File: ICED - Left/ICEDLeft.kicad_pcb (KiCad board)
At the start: 2 copper layers, 175.4 x 145 mm, 162 parts, among them P1 Conn_ARM_JTAG_SWD_10, P2 DX07S024XJ1R1100, P3 CONN_17, P4 692121130100, P5 RGB Out, Q1 TC1264, U1 MK20DX256VLH7, U2 IS31FL3737-QFLS4-TR, X1 CRYSTAL

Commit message: More routing
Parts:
- C18, C19, C20, C21, C6, C8, C9, R12, R3, R4, R5, R8: moved to B.Cu
- moved R5 37.0 mm to (101.6, 130.7), turned to 180 degrees
- moved R3 37.0 mm to (100.2, 130.7), turned to 180 degrees
- moved R4 30.5 mm to (97.8, 122.3)
- moved R8 17.1 mm to (97.1, 78.0), turned to 90 degrees
- moved C18 9.52 mm to (100.2, 69.3), turned to 90 degrees
- moved C20 9.22 mm to (101.9, 78.0)
- moved C21 9.08 mm to (99.6, 78.0)
- moved C9 8.99 mm to (100.7, 78.0)
- moved C6 8.69 mm to (100.2, 70.2), turned to 90 degrees
- moved C19 4.53 mm to (108.2, 75.3), turned to 0 degrees
- moved C8 4.09 mm to (106.4, 75.3), turned to 0 degrees
- moved R12 3.58 mm to (102.7, 75.8), turned to 270 degrees
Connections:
- U2 pad 21: /mcu/ledmatrix_2/Row4A -> /mcu/ledmatrix_2/Row3B
- U2 pad 22: /mcu/ledmatrix_2/Row4B -> /mcu/ledmatrix_2/Row4A
- U2 pad 23: /mcu/ledmatrix_2/Row4C -> /mcu/ledmatrix_2/Row4B
- U2 pad 24: /mcu/ledmatrix_2/Row5A -> /mcu/ledmatrix_2/Row4C
- U2 pad 25: /mcu/ledmatrix_2/Row5B -> /mcu/ledmatrix_2/Row5A
- U2 pad 27: (no net) -> /mcu/ledmatrix_2/Row5B
- U2 pad 29: /mcu/ledmatrix_2/GND -> VSS
- U2 pad 36: /mcu/ledmatrix_2/GND -> VSS
- U2 pad 4: /mcu/ledmatrix_2/GND -> VSS
- U2 pad 40: /mcu/ledmatrix_2/GND -> VSS
- U2 pad 41: /mcu/ledmatrix_2/GND -> VSS
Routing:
- net VSS: track 422.6 -> 612.9 mm, vias 9 -> 17
- net /mcu/ledmatrix_2/Blue3: track 139.7 -> 286.5 mm, vias 6 -> 10
- net /mcu/ledmatrix_2/Green3: track 136.3 -> 281.1 mm, vias 6 -> 10
- net /mcu/ledmatrix_2/Red3: track 124.8 -> 257.8 mm, vias 6 -> 10
- net /mcu/SDB: track 0.00 -> 106.0 mm, vias 0 -> 4
- net /mcu/ledmatrix_2/Blue2: track 248.1 -> 343.8 mm, vias 10 -> 11
- net /mcu/SDA0: track 52.4 -> 135.9 mm, vias 3 -> 6
- net /mcu/SCL0: track 53.5 -> 135.7 mm, vias 3 -> 6
- net /mcu/ledmatrix_2/Green2: track 237.0 -> 316.3 mm, vias 10 -> 11
- net /mcu/RGBIN: track 76.1 -> 0.46 mm, vias 2 -> 0
- net /mcu/ledmatrix_2/Row2B: track 1.27 -> 65.7 mm, vias 1 -> 2
- net /mcu/ledmatrix_2/Row4B: track 0.00 -> 44.9 mm
- net VDD: track 265.9 -> 301.7 mm, vias 7 -> 12
- net /mcu/ledmatrix_2/GND: track 21.9 -> 0.00 mm
- net /mcu/ledmatrix_2/Green4: track 139.8 -> 118.8 mm, vias 9 -> 7
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
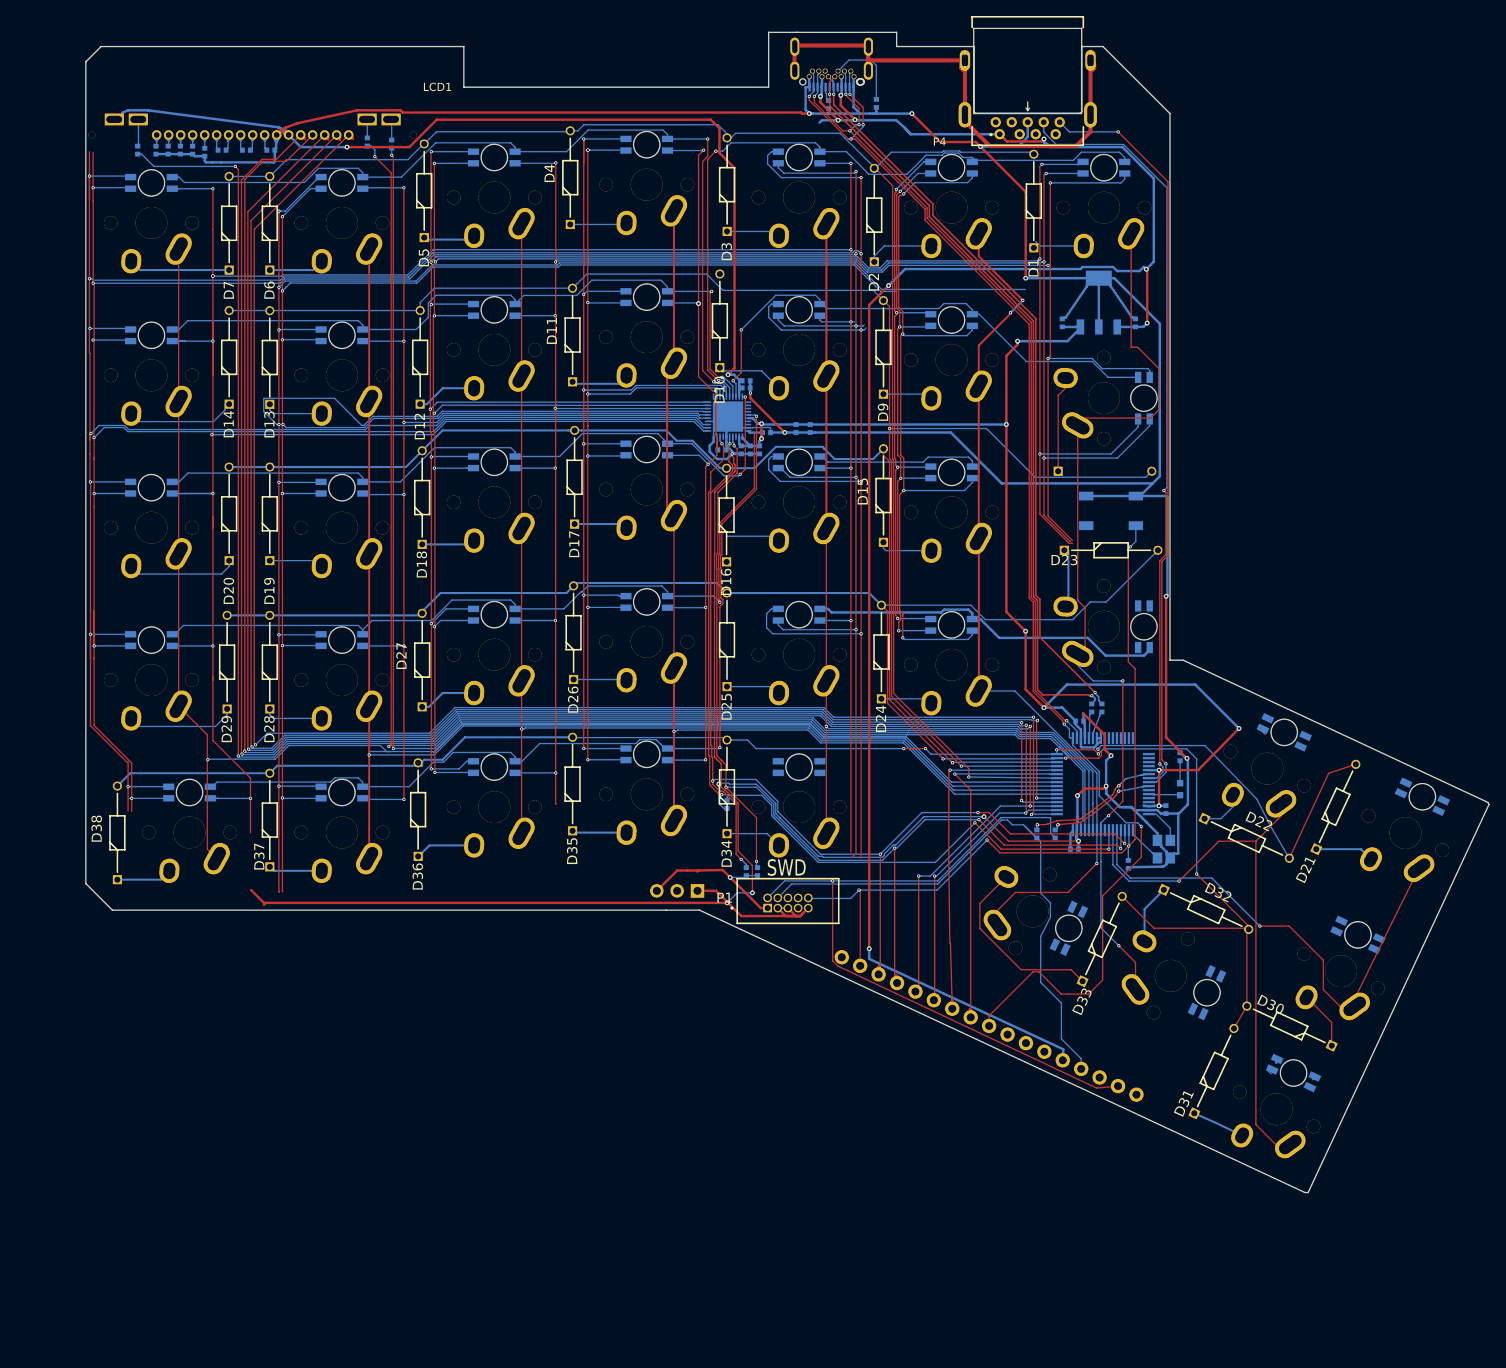
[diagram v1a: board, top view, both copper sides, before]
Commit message: Most non-thumb routing finished
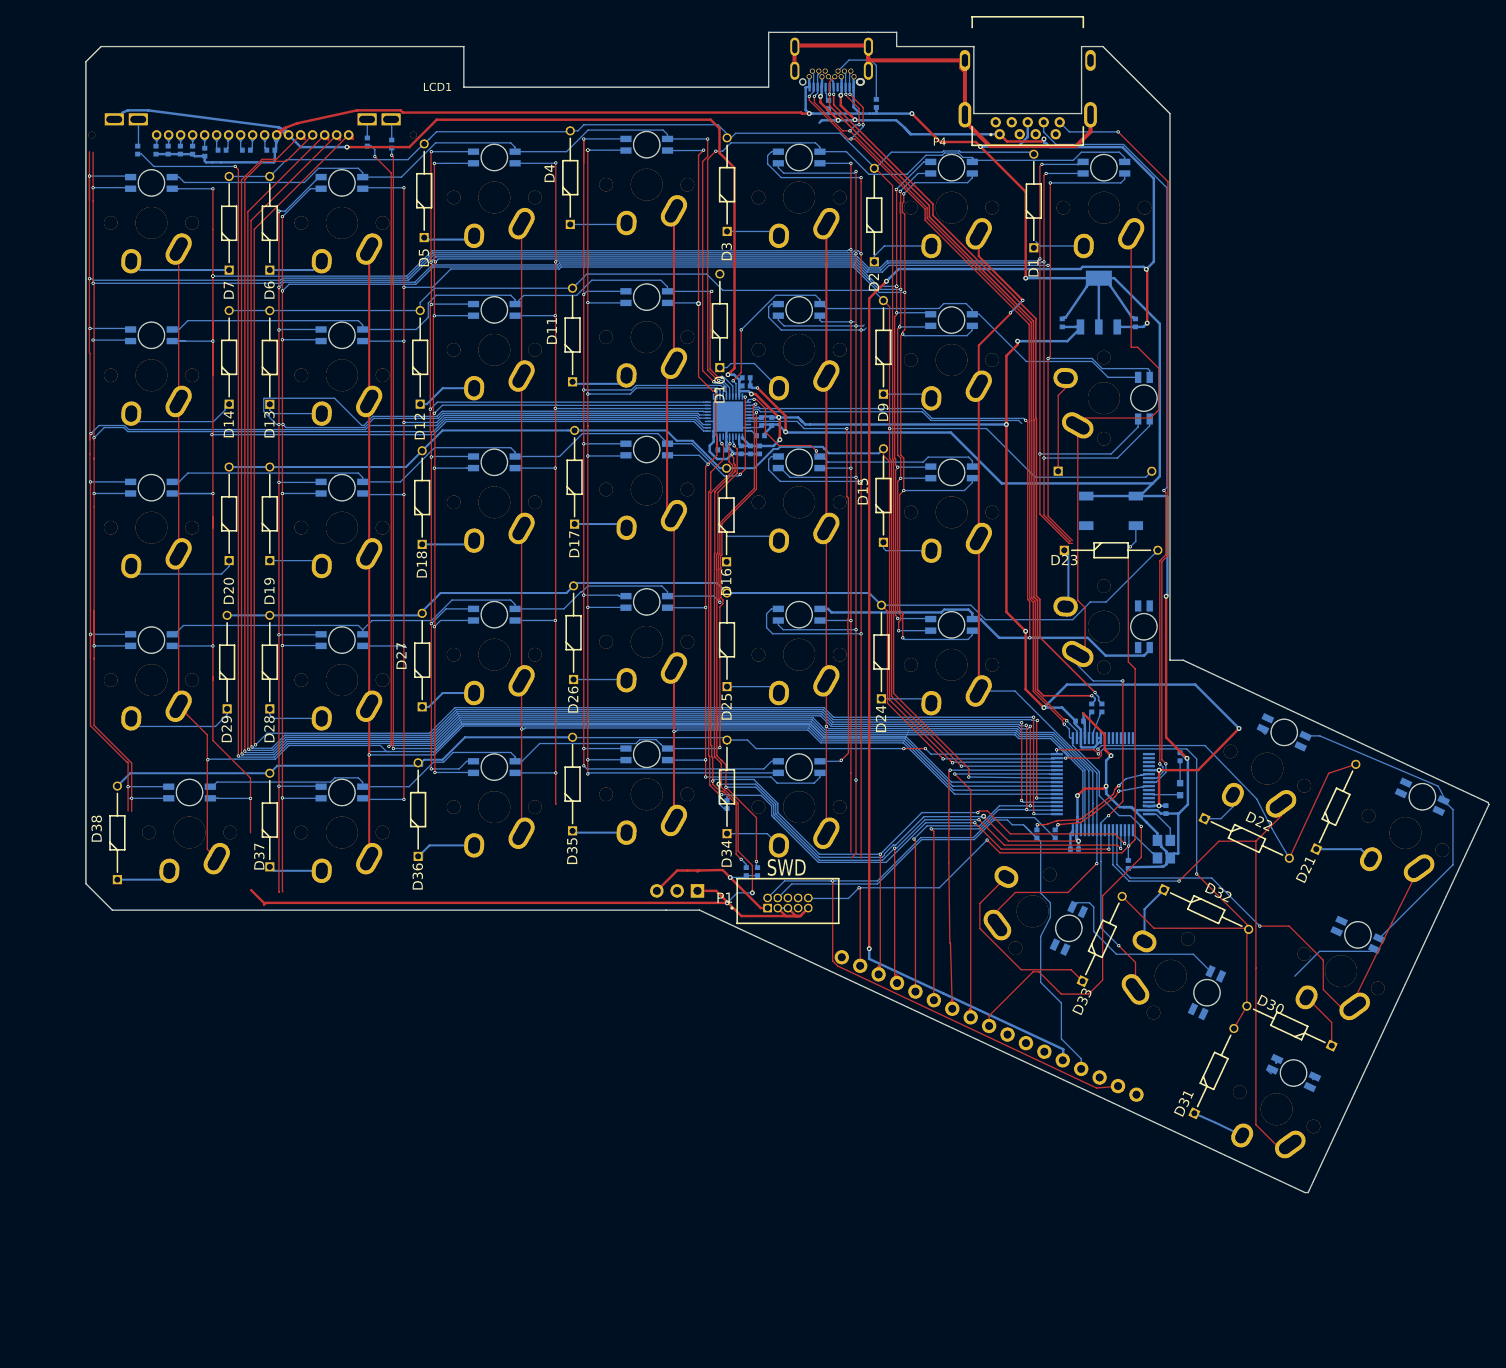
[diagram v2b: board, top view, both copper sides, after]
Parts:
- LCD1: value NHD-C12832A1Z -> VAL**
- moved C19 4.90 mm to (103.4, 74.4)
- moved C8 4.41 mm to (102.1, 74.4)
- moved R12 0.84 mm to (102.0, 76.2)
- moved C18 0.38 mm to (100.2, 69.0)
- moved C6 0.25 mm to (100.2, 70.0)
- turned LED30 to 335 degrees
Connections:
- LED31 pad 1: /mcu/ledmatrix_2/Red4 -> /mcu/ledmatrix_2/Red1
- LED31 pad 2: /mcu/ledmatrix_2/Green4 -> /mcu/ledmatrix_2/Green1
- LED31 pad 3: /mcu/ledmatrix_2/Blue4 -> /mcu/ledmatrix_2/Blue1
- LED32 pad 1: /mcu/ledmatrix_2/Red3 -> /mcu/ledmatrix_2/Red2
- LED32 pad 2: /mcu/ledmatrix_2/Green3 -> /mcu/ledmatrix_2/Green2
- LED32 pad 3: /mcu/ledmatrix_2/Blue3 -> /mcu/ledmatrix_2/Blue2
- LED33 pad 1: /mcu/ledmatrix_2/Red2 -> /mcu/ledmatrix_2/Red3
- LED33 pad 2: /mcu/ledmatrix_2/Green2 -> /mcu/ledmatrix_2/Green3
- LED33 pad 3: /mcu/ledmatrix_2/Blue2 -> /mcu/ledmatrix_2/Blue3
- LED34 pad 1: /mcu/ledmatrix_2/Red1 -> /mcu/ledmatrix_2/Red4
- LED34 pad 2: /mcu/ledmatrix_2/Green1 -> /mcu/ledmatrix_2/Green4
- LED34 pad 3: /mcu/ledmatrix_2/Blue1 -> /mcu/ledmatrix_2/Blue4
- P4 pad S4: /GND -> (no net)
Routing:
- net /mcu/ledmatrix_2/Row5B: track 0.69 -> 81.2 mm, vias 0 -> 2
- net /mcu/ledmatrix_2/Row4C: track 0.00 -> 76.4 mm
- net /mcu/ledmatrix_2/Red2: track 236.3 -> 301.0 mm, vias 10 -> 12
- net /mcu/ledmatrix_2/Row4B: track 44.9 -> 107.8 mm, vias 0 -> 2
- net /mcu/ledmatrix_2/Blue4: track 125.0 -> 152.0 mm, vias 6 -> 7
- net /mcu/ledmatrix_2/Green4: track 118.8 -> 144.0 mm, vias 7 -> 8
- net /mcu/ledmatrix_2/Red4: track 103.8 -> 121.0 mm, vias 6 -> 7
- net /mcu/ledmatrix_2/Blue2: track 343.8 -> 327.4 mm, vias 11 -> 13
- net /mcu/ledmatrix_2/Row3B: track 20.5 -> 35.0 mm, vias 0 -> 2
- net /mcu/ledmatrix_2/Red3: track 257.8 -> 269.2 mm
- net VDD: track 301.7 -> 311.3 mm, vias 12 -> 13
- net /GND: track 64.3 -> 57.0 mm
- net /mcu/ledmatrix_2/Row4A: track 97.6 -> 102.4 mm, vias 1 -> 2
- net VSS: track 612.9 -> 616.9 mm
- net /mcu/SCLK: track 227.8 -> 231.4 mm
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
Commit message: Routed and DRC passes
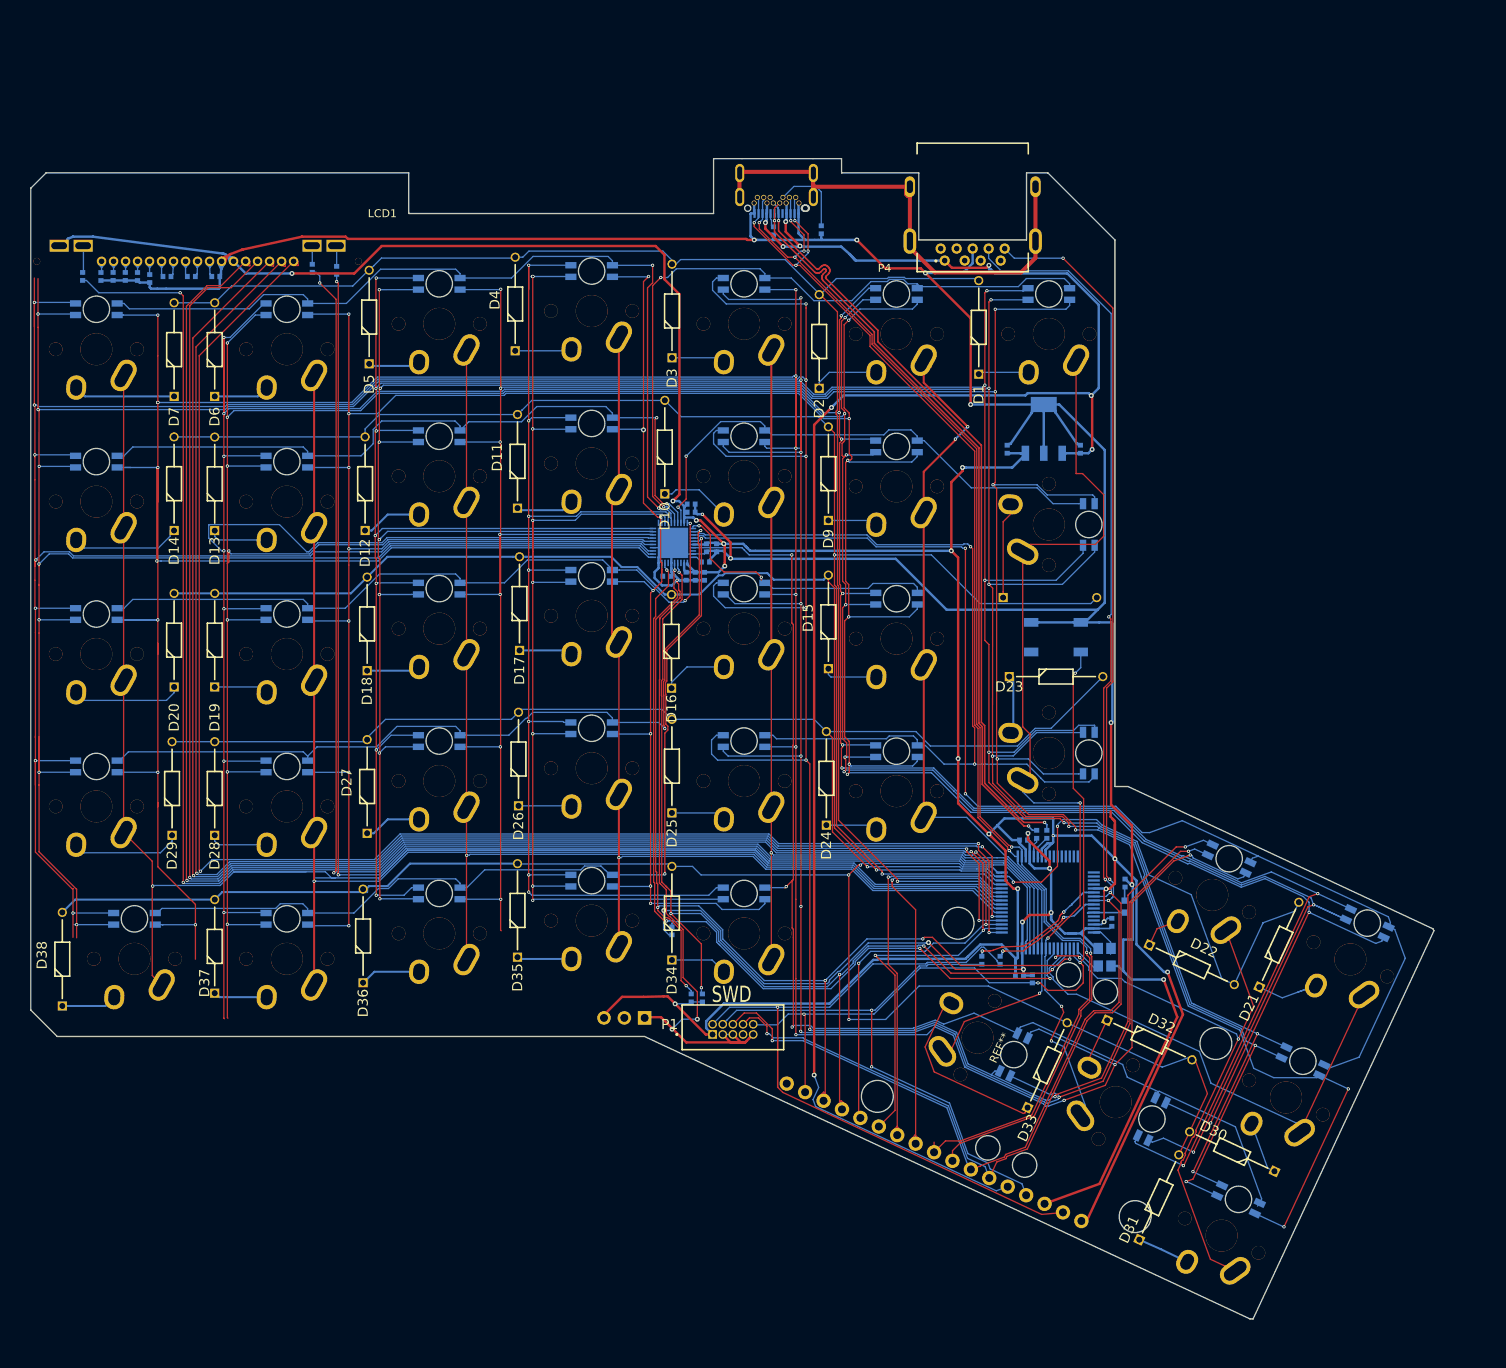
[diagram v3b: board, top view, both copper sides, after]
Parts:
- added REF**: Stabilizer_Cherry_MX_2u, prettylib:Stabilizer_Cherry_MX_2u, F.Cu at (129.1, 151.5)
- added STAB1: Stabilizer_Cherry_MX_2u, prettylib:Stabilizer_Cherry_MX_2u, F.Cu at (146.4, 159.5)
- LCD1: value VAL** -> NHD-C12832A1Z
- moved C5 18.7 mm to (136.0, 144.1), turned to 0 degrees
- moved D21 18.7 mm to (164.3, 145.1)
- moved D32 17.8 mm to (145.3, 149.3)
- moved D30 17.3 mm to (166.2, 168.2)
- moved S26 17.2 mm to (80.9, 117.8)
- moved R5 17.2 mm to (94.7, 146.5)
- moved LED1 17.2 mm to (138.0, 58.5)
- moved C13 17.2 mm to (25.6, 56.6)
- moved D12 17.2 mm to (52.6, 88.1)
- moved S31 17.2 mm to (159.6, 176.2)
- moved D33 17.2 mm to (135.4, 160.2)
- moved S25 17.2 mm to (99.9, 119.4)
- moved P2 17.2 mm to (100.4, 47.8)
- moved S4 17.2 mm to (80.9, 60.6)
- moved LED24 17.2 mm to (119.0, 115.6)
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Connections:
- LED31 pad 1: /mcu/ledmatrix_2/Red1 -> /mcu/ledmatrix_2/Red3
- LED31 pad 2: /mcu/ledmatrix_2/Green1 -> /mcu/ledmatrix_2/Green3
- LED31 pad 3: /mcu/ledmatrix_2/Blue1 -> /mcu/ledmatrix_2/Blue3
- LED33 pad 1: /mcu/ledmatrix_2/Red3 -> /mcu/ledmatrix_2/Red1
- LED33 pad 2: /mcu/ledmatrix_2/Green3 -> /mcu/ledmatrix_2/Green1
- LED33 pad 3: /mcu/ledmatrix_2/Blue3 -> /mcu/ledmatrix_2/Blue1
- P3 pad 17: /mcu/RGBIN -> (no net)
- P4 pad S4: (no net) -> /GND
- U1 pad 26: /mcu/RGBIN -> (no net)
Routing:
- net /mcu/ledmatrix_2/Blue2: track 327.4 -> 455.5 mm, vias 13 -> 15
- net /mcu/ledmatrix_2/Red1: track 368.8 -> 492.2 mm, vias 13 -> 17
- net /mcu/ledmatrix_2/Green2: track 316.5 -> 435.5 mm, vias 12 -> 15
- net /mcu/ledmatrix_2/Red2: track 301.0 -> 413.8 mm, vias 12 -> 15
- net VDD: track 311.3 -> 423.1 mm, vias 13 -> 16
- net /mcu/ledmatrix_2/Red3: track 269.2 -> 379.8 mm, vias 10 -> 14
- net /mcu/ledmatrix_2/Blue3: track 286.5 -> 393.2 mm, vias 10 -> 14
- net /mcu/ledmatrix_2/Green3: track 281.1 -> 386.1 mm, vias 10 -> 14
- net /mcu/ledmatrix_2/Green1: track 418.4 -> 516.0 mm, vias 13 -> 16
- net /mcu/ledmatrix_2/Blue1: track 440.1 -> 525.5 mm, vias 12 -> 15
- net /mcu/TX0: track 93.6 -> 177.8 mm, vias 2 -> 4
- net /mcu/RX0: track 95.7 -> 179.7 mm, vias 2 -> 4
- net /mcu/ledmatrix_2/Row4C: track 76.4 -> 149.0 mm, vias 0 -> 2
- net /mcu/ledmatrix_2/Row5B: track 81.2 -> 148.8 mm, vias 2 -> 3
- net /mcu/RX1: track 106.8 -> 158.0 mm, vias 5 -> 6
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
